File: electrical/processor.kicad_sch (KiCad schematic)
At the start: 28 parts, among them IC1 STM32G484QET6, J1 FTSH-107-01-F-DV-K, SW1 SW_DPDT_x2, Y1 32.764KHz, Y2 24MHz

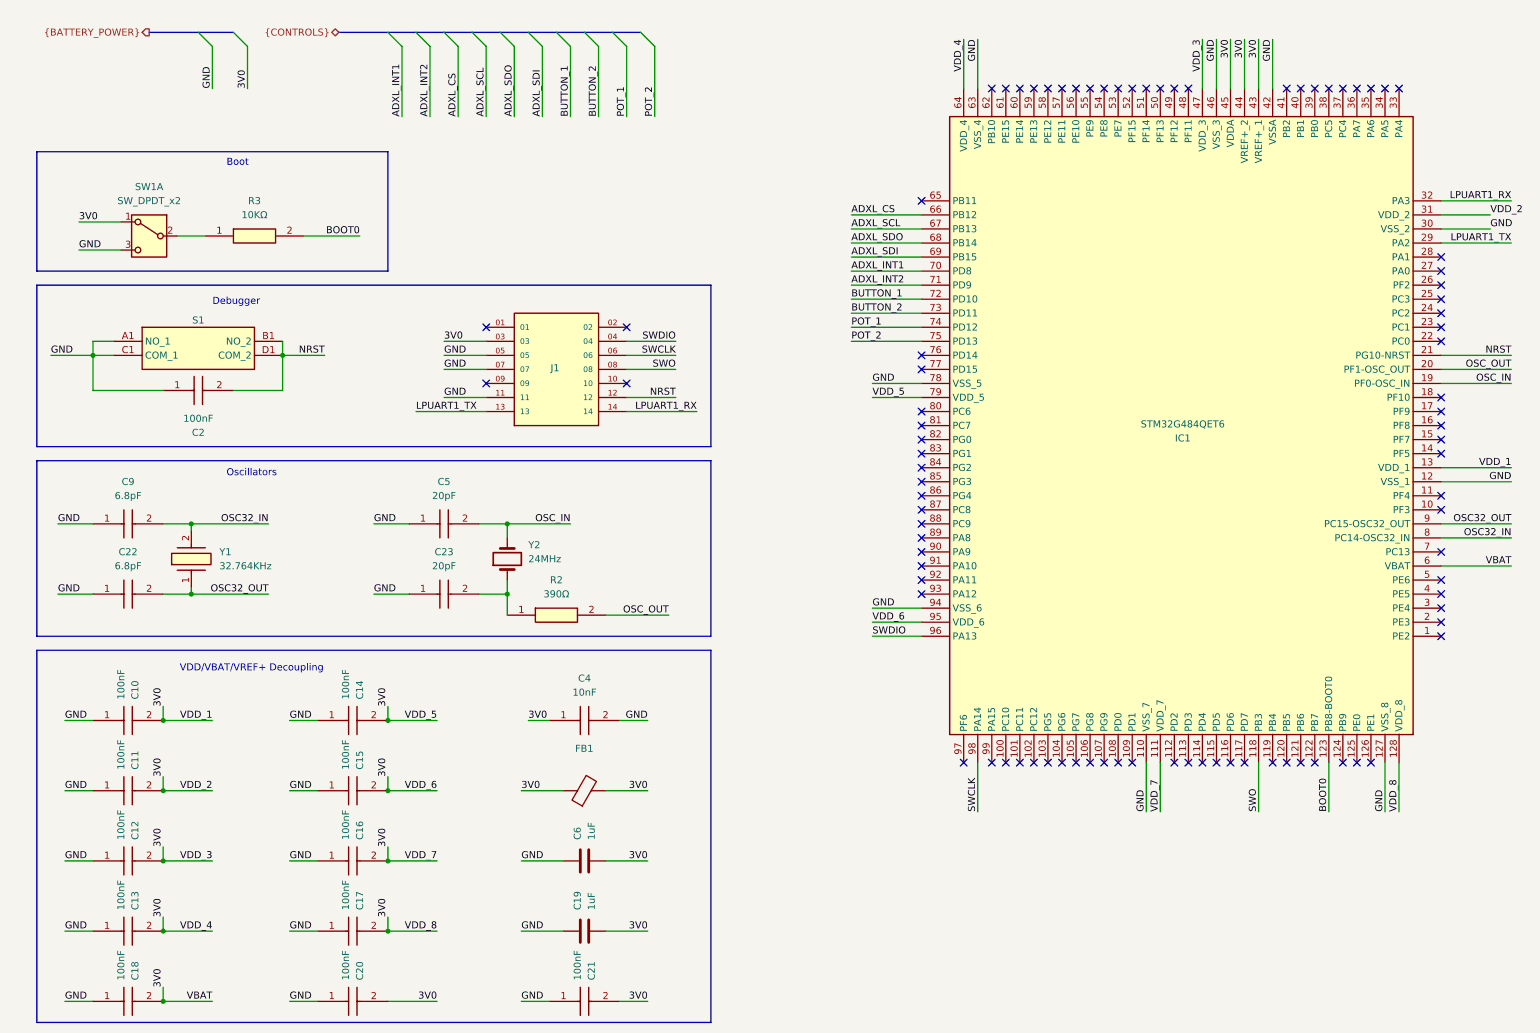
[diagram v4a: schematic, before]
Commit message: #3 Adding WiFi module to the schematic.
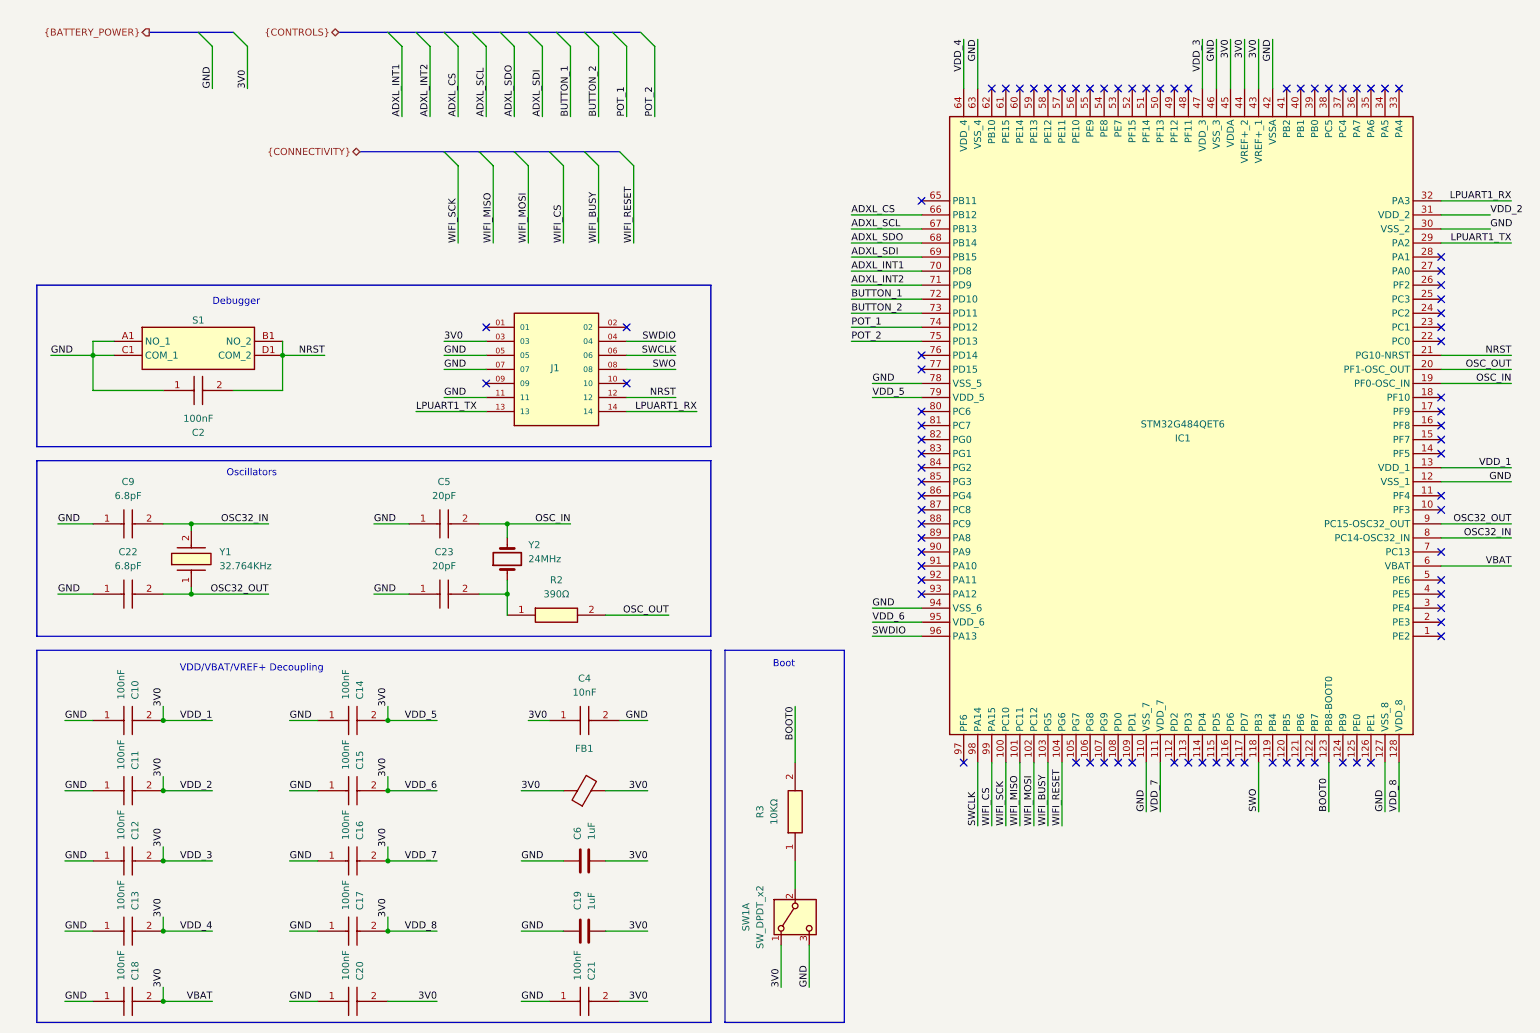
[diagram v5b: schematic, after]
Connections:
- net WIFI_SCK: now reaches IC1.100 (PC10)
- net WIFI_MISO: now reaches IC1.101 (PC11)
- net WIFI_MOSI: now reaches IC1.102 (PC12)
- net WIFI_BUSY: now reaches IC1.103 (PG5)
- net WIFI_RESET: now reaches IC1.104 (PG6)
- net WIFI_CS: now reaches IC1.99 (PA15)
- no-connect marks 90 -> 84
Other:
- moved on the sheet: R3, SW1A

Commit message: #3 Updating schematic.
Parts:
- removed C19, C6: 1uF, symbol Device:C
- removed C2: 100nF, SamacSys_Parts:MAJx16, symbol SamacSys_Parts:MAJCH168BB7104KTEA01
- removed C23, C5: 20pF, SamacSys_Parts:CAPC1608X90N, symbol SamacSys_Parts:06031A200KAT2A
- removed FB1: FerriteBead, symbol Device:FerriteBead
- removed R2: 390Ω, SamacSys_Parts:RESC1608X58N, symbol SamacSys_Parts:MCT0603MD3900BP500
- removed S1: PTS125SM73SMTR21M_LFS, SamacSys_Parts:PTS125SM73SMTR21MLFS, symbol SamacSys_Parts:PTS125SM73SMTR21M_LFS
- removed Y2: 24MHz, symbol Device:Crystal
- added C2, C6: 1uF, SamacSys_Parts:MAJx16, symbol SamacSys_Parts:MAJCT168BB7105KTEA01
- added C32, C33: 20pF, SamacSys_Parts:CAPC1608X90N, symbol SamacSys_Parts:06031A200KAT2A
- added C5: 100nF, SamacSys_Parts:MAJx16, symbol SamacSys_Parts:MAJCH168BB7104KTEA01
- added FB1: ~, SamacSys_Parts:BMCQ1E0000H, symbol SamacSys_Parts:BMC-Q1E0000H
- added R10: 390Ω, SamacSys_Parts:RESC1608X58N, symbol SamacSys_Parts:MCT0603MD3900BP500
- added S4: PTS125SM73SMTR21M_LFS, SamacSys_Parts:PTS125SM73SMTR21MLFS, symbol SamacSys_Parts:PTS125SM73SMTR21M_LFS
- added Y3: 24 MHz, SamacSys_Parts:CX3225FB24000C0FZZH1, symbol SamacSys_Parts:CX3225FB24000C0FZZH1
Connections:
- net 3V0: now also C2.2, C6.2, FB1.1, FB1.2
- net GND: now also C2.1, C32.1, C33.1, C5.2, C6.1, S4.C1 (COM_1), S4.D1 (COM_2), Y3.2 (GND), Y3.4 (GND)
- net NRST: now also C5.1, S4.A1 (NO_1), S4.B1 (NO_2)
- net OSC_IN: now also C32.2, Y3.1 (IO)
- net OSC_OUT: now also R10.2
- net SCREEN_SCL: now reaches IC1.1 (PE2)
- net SCREEN_BUSY: now reaches IC1.2 (PE3)
- net SCREEN_CS: now reaches IC1.3 (PE4)
- net SCREEN_D_C: now reaches IC1.4 (PE5)
- net SCREEN_SDA: now reaches IC1.5 (PE6)
- net SCREEN_RST: now reaches IC1.7 (PC13)
- new net: C33.2, R10.1, Y3.3 (IO)
- no-connect marks 84 -> 78
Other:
- moved on the sheet: J1

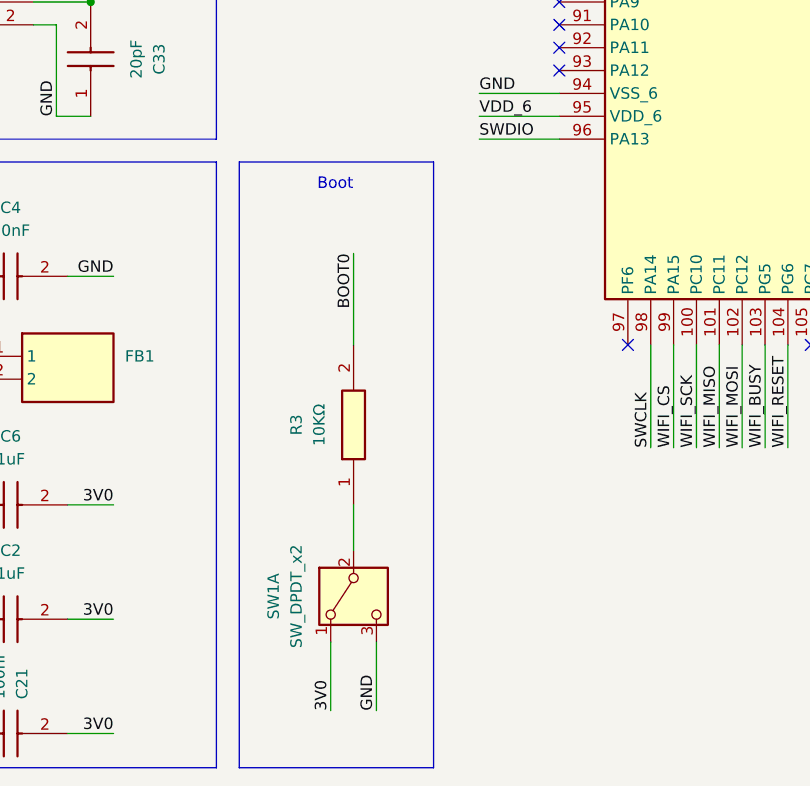
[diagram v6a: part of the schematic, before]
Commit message: #3 Finding CAD for switch.
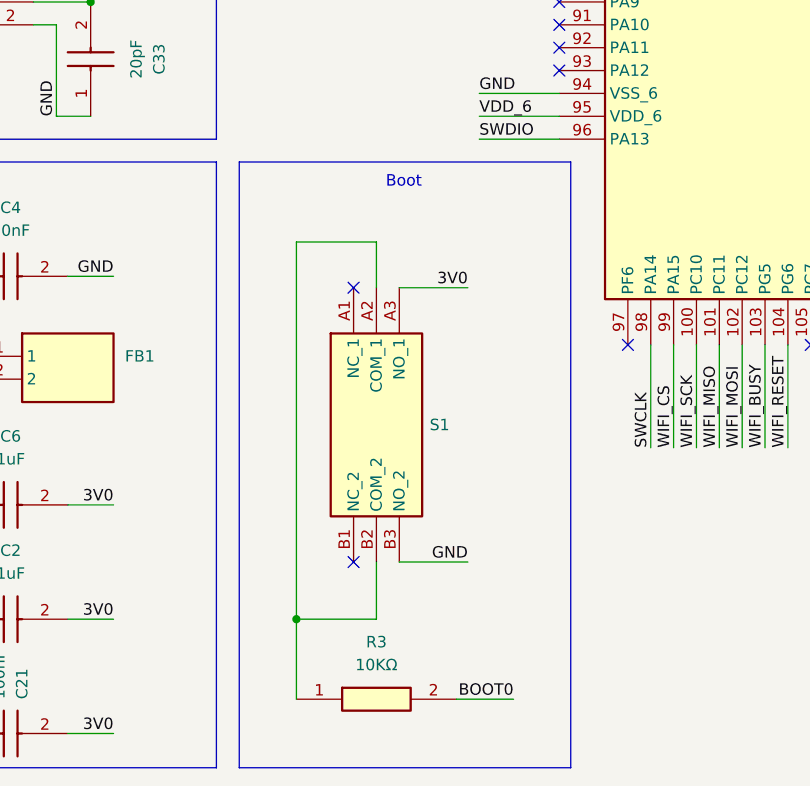
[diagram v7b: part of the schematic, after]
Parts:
- removed SW1: SW_DPDT_x2, symbol Switch:SW_DPDT_x2
- added S1: MHSS1104, SamacSys_Parts:MHSS1104, symbol SamacSys_Parts:MHSS1104
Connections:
- net 3V0: now also S1.A3 (NO_1)
- net GND: now also S1.B3 (NO_2)
- net at R3.1: now also S1.A2 (COM_1), S1.B2 (COM_2)
- no-connect marks 78 -> 80
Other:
- moved on the sheet: R3
